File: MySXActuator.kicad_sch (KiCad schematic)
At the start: 38 parts, among them J1 8P8C, Q1 2N7002, Q2 IRFR7546PbF, Q3 IRFR7546PbF, Q4 2N7002, U1 AP63205WU

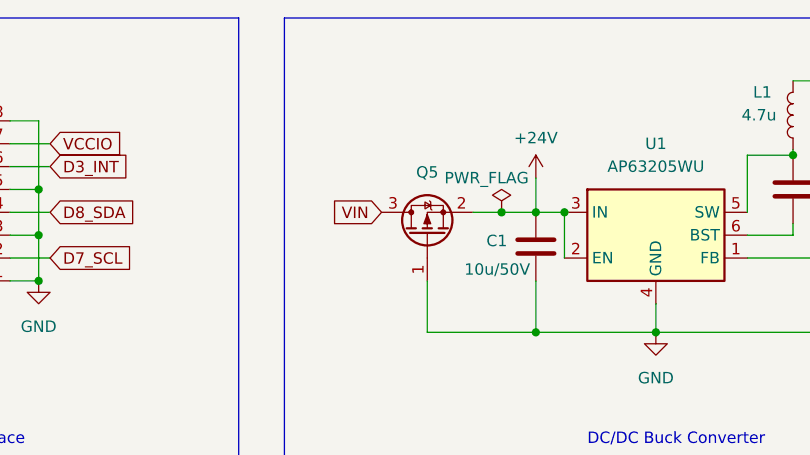
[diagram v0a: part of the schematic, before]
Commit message: update to new kicad version 8.0
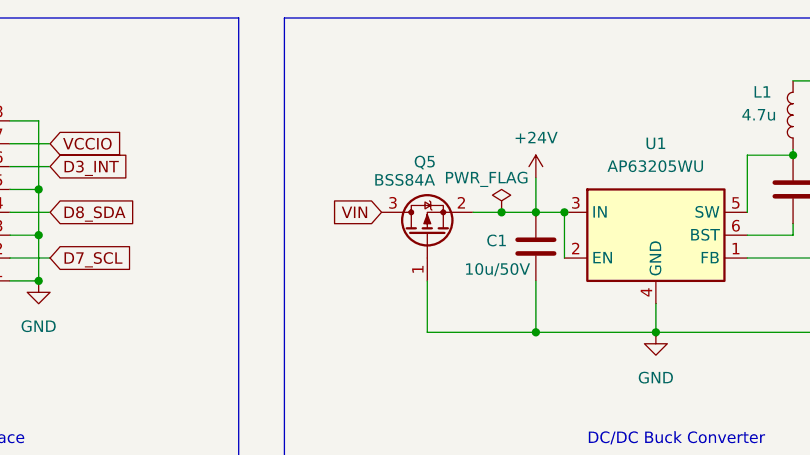
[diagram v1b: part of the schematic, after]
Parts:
- Q5: value ~ -> BSS84A

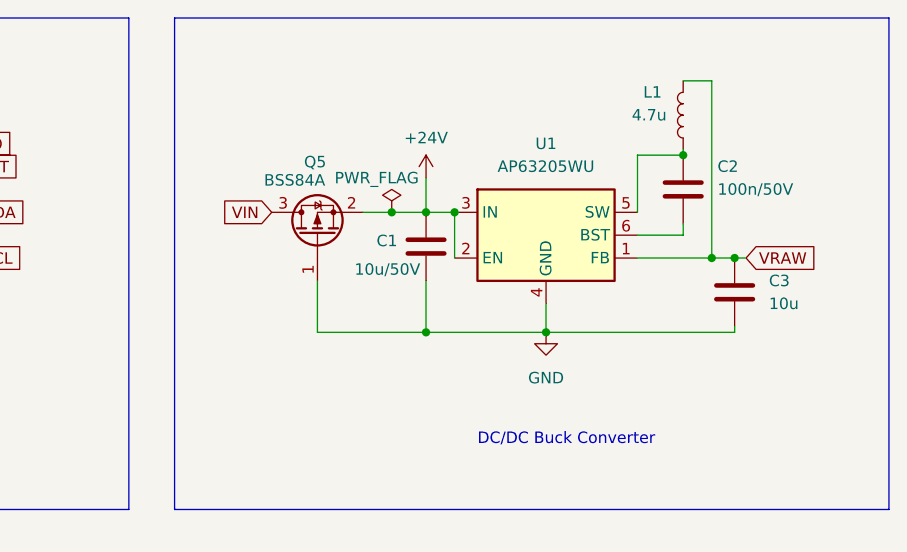
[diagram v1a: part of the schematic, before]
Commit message: add input voltage transient protection
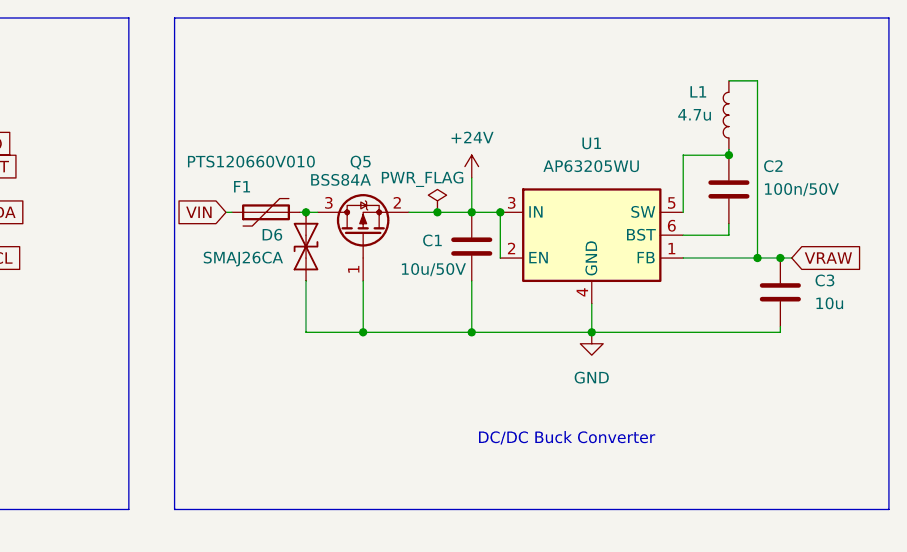
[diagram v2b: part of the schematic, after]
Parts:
- added D6: SMAJ26CA, Diode_SMD:D_SMA, symbol Diode:SMAJ11CA
- added F1: PTS120660V010, Fuse:Fuse_1206_3216Metric_Pad1.42x1.75mm_HandSolder, symbol Device:Polyfuse
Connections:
- net GND: now also D6.1 (A1)
- net VIN: now also F1.1; no longer Q5.3 (D)
- new net: D6.2 (A2), F1.2, Q5.3 (D)
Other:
- moved on the sheet: C1, C2, C3, L1, Q5, U1

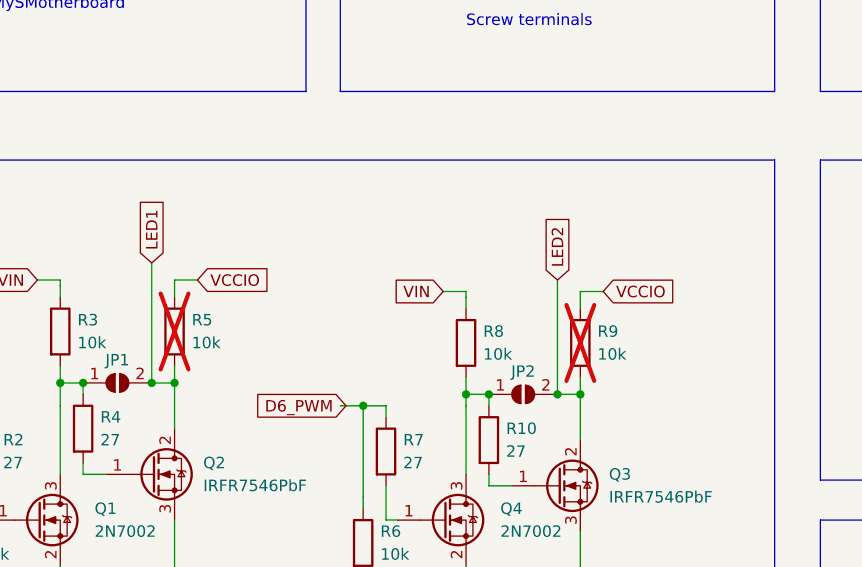
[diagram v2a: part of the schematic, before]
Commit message: add resistors to prevent led glowing when turned off
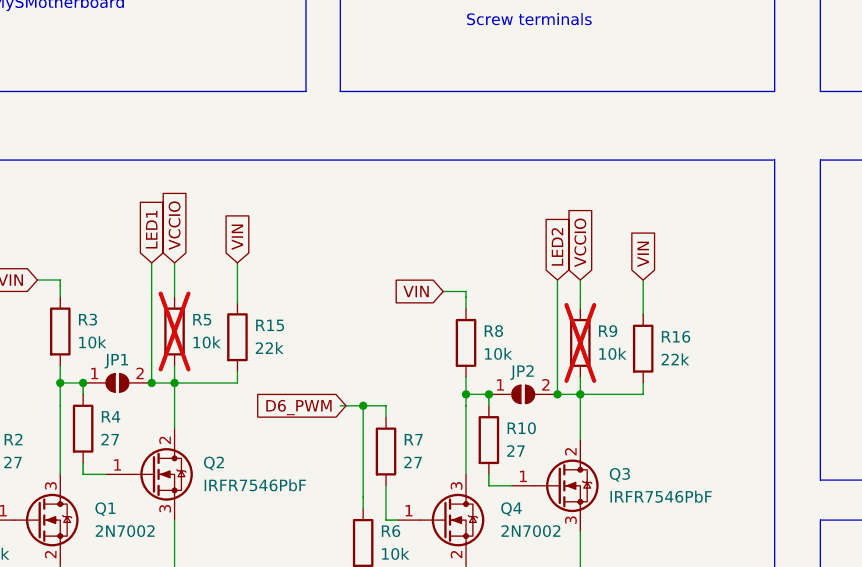
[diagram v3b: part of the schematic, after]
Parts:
- added R15, R16: 22k, Resistor_SMD:R_0603_1608Metric, symbol Device:R
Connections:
- net LED1: now also R15.2
- net LED2: now also R16.2
- net VIN: now also R15.1, R16.1
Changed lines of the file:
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@@
 	(wire
 		(pts
+			(xy 112.395 108.585) (xy 112.395 107.315)
+		)
+		(stroke
+			(width 0.1524)
+			(type solid)
+		)
+	)
+	(wire
+		(pts
 			(xy 73.025 132.715) (xy 81.28 132.715)
 		)
@@
 	(wire
 		(pts
-			(xy 105.41 97.155) (xy 105.41 97.79)
+			(xy 105.41 95.885) (xy 105.41 97.79)
 		)
 		(stroke
@@
 	(wire
 		(pts
+			(xy 60.325 107.315) (xy 67.31 107.315)
+		)
+		(stroke
+			(width 0.1524)
+			(type solid)
+		)
+	)
+	(wire
+		(pts
 			(xy 60.325 122.555) (xy 60.325 132.715)
 		)
@@
 	(wire
 		(pts
+			(xy 105.41 108.585) (xy 112.395 108.585)
+		)
+		(stroke
+			(width 0.1524)
+			(type solid)
+		)
+	)
+	(wire
+		(pts
 			(xy 47.625 95.885) (xy 45.085 95.885)
 		)
@@
 	(wire
 		(pts
-			(xy 60.325 95.885) (xy 60.325 97.79)
+			(xy 60.325 93.98) (xy 60.325 97.79)
 		)
 		(stroke
@@
 	(wire
 		(pts
+			(xy 67.31 93.98) (xy 67.31 98.425)
+		)
+		(stroke
+			(width 0)
+			(type default)
+		)
+	)
+	(wire
+		(pts
 			(xy 198.12 136.525) (xy 198.12 137.16)
 		)
@@
 	(wire
 		(pts
-			(xy 107.95 97.155) (xy 105.41 97.155)
-		)
-		(stroke
-			(width 0.1524)
-			(type solid)
-		)
-	)
-	(wire
-		(pts
 			(xy 198.12 105.41) (xy 205.105 105.41)
 		)
@@
 	(wire
 		(pts
-			(xy 62.865 95.885) (xy 60.325 95.885)
-		)
-		(stroke
-			(width 0.1524)
-			(type solid)
-		)
-	)
-	(wire
-		(pts
 			(xy 40.64 50.165) (xy 36.195 50.165)
 		)
@@
 		)
 	)
+	(wire
+		(pts
+			(xy 112.395 95.885) (xy 112.395 99.695)
+		)
+		(stroke
+			(width 0)
+			(type default)
+		)
+	)
+	(wire
+		(pts
+			(xy 67.31 107.315) (xy 67.31 106.045)
+		)
+		(stroke
+			(width 0.1524)
+			(type solid)
+		)
+	)
 	(rectangle
 		(start 132.08 82.55)
@@
 		)
 	)
+	(global_label "VIN"
+		(shape input)
+		(at 112.395 95.885 90)
+		(fields_autoplaced yes)
+		(effects
+			(font
+				(size 1.27 1.27)
+			)
+			(justify left)
+		)
+		(property "Intersheetrefs" "${INTERSHEET_REFS}"
+			(at 112.395 89.8759 90)
+			(effects
+				(font
+					(size 1.27 1.27)
+				)
+				(justify left)
+				(hide yes)
+			)
+		)
+	)
 	(global_label "VRAW"
 		(shape input)
@@
 	(global_label "VCCIO"
 		(shape input)
-		(at 107.95 97.155 0)
+		(at 105.41 95.885 90)
 		(fields_autoplaced yes)
 		(effects
@@
 		)
 		(property "Intersheetrefs" "${INTERSHEET_REFS}"
-			(at 116.4991 97.155 0)
+			(at 105.41 87.3359 90)
 			(effects
 				(font
@@
 		)
 	)
+	(global_label "VIN"
+		(shape input)
+		(at 67.31 93.98 90)
+		(fields_autoplaced yes)
+		(effects
+			(font
+				(size 1.27 1.27)
+			)
+			(justify left)
+		)
+		(property "Intersheetrefs" "${INTERSHEET_REFS}"
+			(at 67.31 87.9709 90)
+			(effects
+				(font
+					(size 1.27 1.27)
+				)
+				(justify left)
+				(hide yes)
+			)
+		)
+	)
 	(global_label "SW2"
 		(shape input)
@@
 	(global_label "VCCIO"
 		(shape input)
-		(at 62.865 95.885 0)
+		(at 60.325 93.98 90)
 		(fields_autoplaced yes)
 		(effects
@@
 		)
 		(property "Intersheetrefs" "${INTERSHEET_REFS}"
-			(at 71.4141 95.885 0)
+			(at 60.325 85.4309 90)
 			(effects
 				(font
@@
 	)
 	(symbol
+		(lib_id "Device:R")
+		(at 112.395 103.505 0)
+		(unit 1)
+		(exclude_from_sim no)
+		(in_bom yes)
+		(on_board yes)
+		(dnp no)
+		(fields_autoplaced yes)
+		(property "Reference" "R16"
+			(at 114.3 102.235 0)
+			(effects
+				(font
+					(size 1.27 1.27)
+				)
+				(justify left)
+			)
+		)
+		(property "Value" "22k"
+			(at 114.3 104.775 0)
+			(effects
+				(font
+					(size 1.27 1.27)
+				)
+				(justify left)
+			)
+		)
+		(property "Footprint" "Resistor_SMD:R_0603_1608Metric"
+			(at 110.617 103.505 90)
+			(effects
+				(font
+					(size 1.27 1.27)
+				)
+				(hide yes)
+			)
+		)
+		(property "Datasheet" "~"
+			(at 112.395 103.505 0)
+			(effects
+				(font
+					(size 1.27 1.27)
+				)
+				(hide yes)
+			)
+		)
+		(property "Description" ""
+			(at 112.395 103.505 0)
+			(effects
+				(font
+					(size 1.27 1.27)
+				)
+				(hide yes)
+			)
+		)
+		(pin "2"
+		)
+		(pin "1"
+		)
+		(instances
+			(project "MySXActuator"
+				(path "/57392524-8f0a-44f4-94e8-a8a5959d46fa"
+					(reference "R16")
+					(unit 1)
+				)
+			)
+		)
+	)
+	(symbol
 		(lib_id "Device:Polyfuse")
 		(at 205.105 41.91 90)
@@
 					(unit 1)
 				)
+			)
+		)
+	)
+	(symbol
+		(lib_id "Device:R")
+		(at 67.31 102.235 0)
+		(unit 1)
+		(exclude_from_sim no)
+		(in_bom yes)
+		(on_board yes)
+		(dnp no)
+		(fields_autoplaced yes)
+		(property "Reference" "R15"
+			(at 69.215 100.965 0)
+			(effects
+				(font
+					(size 1.27 1.27)
+				)
+				(justify left)
+			)
+		)
+		(property "Value" "22k"
+			(at 69.215 103.505 0)
+			(effects
+				(font
+					(size 1.27 1.27)
+				)
+				(justify left)
+			)
+		)
+		(property "Footprint" "Resistor_SMD:R_0603_1608Metric"
+			(at 65.532 102.235 90)
+			(effects
+				(font
+					(size 1.27 1.27)
+				)
+				(hide yes)
+			)
+		)
+		(property "Datasheet" "~"
+			(at 67.31 102.235 0)
+			(effects
+				(font
+					(size 1.27 1.27)
+				)
+				(hide yes)
+			)
+		)
+		(property "Description" ""
+			(at 67.31 102.235 0)
+			(effects
+				(font
+					(size 1.27 1.27)
+				)
+				(hide yes)
+			)
+		)
+		(pin "2"
+		)
+		(pin "1"
+		)
+		(instances
+			(project "MySXActuator"
+				(path "/57392524-8f0a-44f4-94e8-a8a5959d46fa"
+					(reference "R15")
+					(unit 1)
+				)
